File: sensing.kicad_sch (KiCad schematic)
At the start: 0 parts

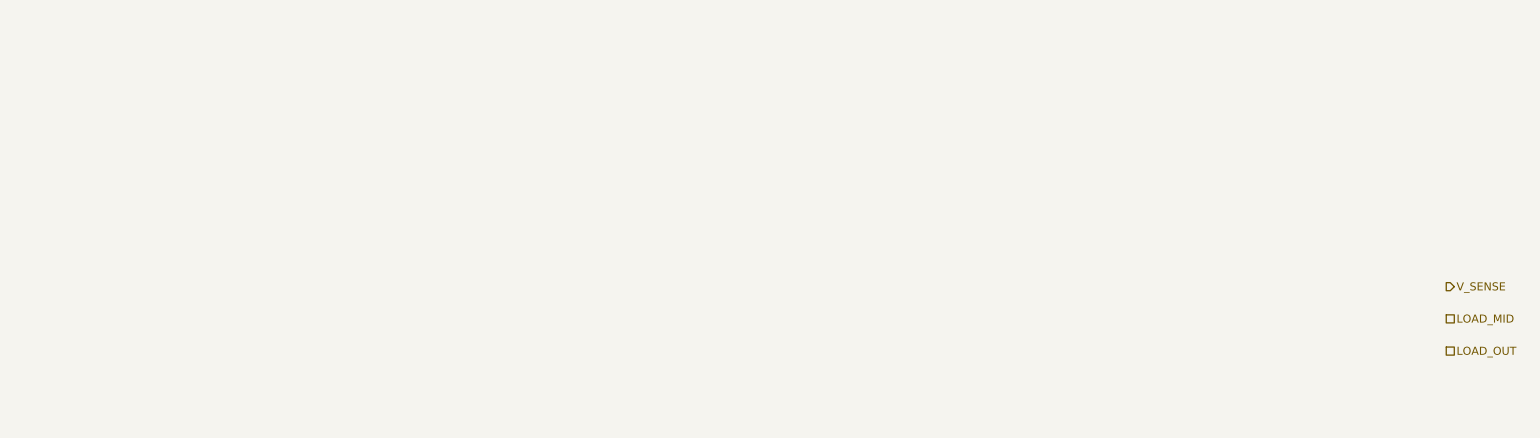
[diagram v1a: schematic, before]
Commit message: Add current sensing sheet
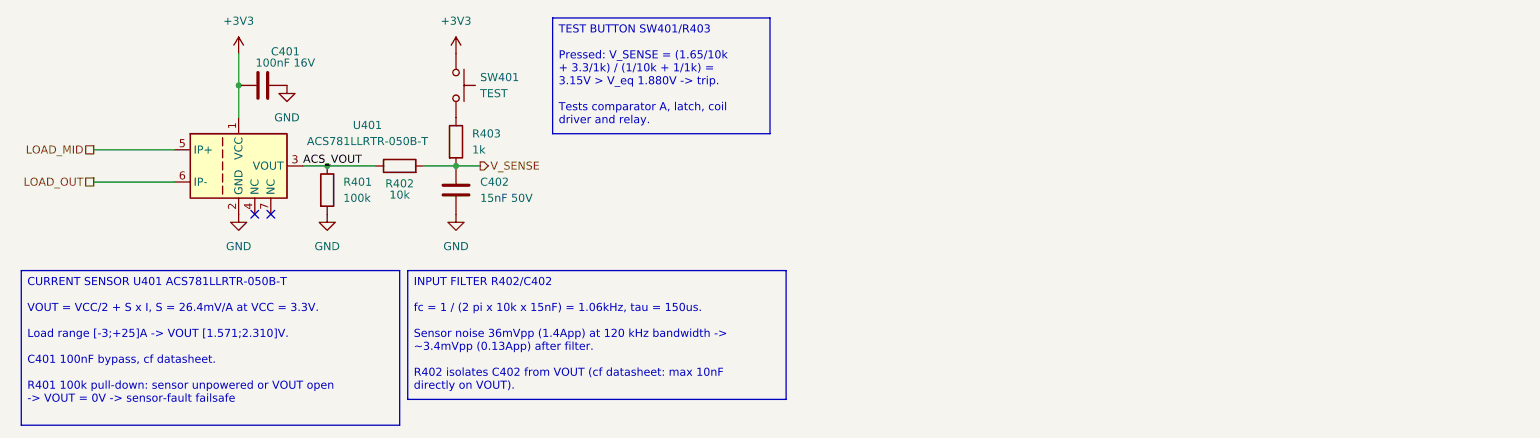
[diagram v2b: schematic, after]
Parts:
- added C401: 100nF 16V, Capacitor_SMD:C_0603_1608Metric, symbol Device:C
- added C402: 15nF 50V, Capacitor_SMD:C_0603_1608Metric, symbol Device:C
- added R401: 100k, Resistor_SMD:R_0603_1608Metric, symbol Device:R
- added R402: 10k, Resistor_SMD:R_0603_1608Metric, symbol Device:R
- added R403: 1k, Resistor_SMD:R_0603_1608Metric, symbol Device:R
- added SW401: TEST, Button_Switch_SMD:Nidec_Copal_CAS-120A, symbol Switch:SW_Push
- added U401: ACS781LLRTR-050B-T, Sensor_Current:Allegro_PSOF-7_4.8x6.4mm_P1.60mm, symbol monitor:ACS781LLRTR-050B-T
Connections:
- net LOAD_MID: now also U401.5 (IP+)
- net LOAD_OUT: now also U401.6 (IP-)
- net V_SENSE: now also C402.1, R402.2, R403.2
- new net: R403.1, SW401.2
- new net +3V3: C401.1, SW401.1, U401.1 (VCC)
- new net ACS_VOUT: R401.1, R402.1, U401.3 (VOUT)
- new net GND: C401.2, C402.2, R401.2, U401.2 (GND)
- no-connect marks 0 -> 2

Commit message: Add current sensing sheet
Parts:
- added TP401: V_SENSE, TestPoint:TestPoint_Pad_D1.5mm, symbol Connector:TestPoint
- C402: value 15nF 50V -> 15nF 50V C0G
- SW401: footprint Button_Switch_SMD:Nidec_Copal_CAS-120A -> Button_Switch_SMD:SW_SPST_PTS645Sx43SMTR92
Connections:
- net V_SENSE: now also TP401.1
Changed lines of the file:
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@@
+		(color 0 0 0 0)
+	)
+	(junction
+		(at 100.33 38.1)
+		(diameter 0)
 		(color 0 0 0 0)
 	)
@@
 	(wire
 		(pts
-			(xy 88.9 38.1) (xy 85.09 38.1)
+			(xy 100.33 38.1) (xy 85.09 38.1)
+		)
+		(stroke
+			(width 0)
+			(type default)
+		)
+	)
+	(wire
+		(pts
+			(xy 105.41 38.1) (xy 100.33 38.1)
 		)
 		(stroke
@@
 	(hierarchical_label "V_SENSE"
 		(shape output)
-		(at 88.9 38.1 0)
+		(at 105.41 38.1 0)
 		(effects
 			(font
@@
 			)
 		)
-		(property "Footprint" "Button_Switch_SMD:Nidec_Copal_CAS-120A"
+		(property "Footprint" "Button_Switch_SMD:SW_SPST_PTS645Sx43SMTR92"
 			(at 90.17 25.4 0)
 			(hide yes)
@@
 			)
 		)
-		(property "Value" "15nF 50V"
+		(property "Value" "15nF 50V C0G"
 			(at 88.9 43.1799 0)
 			(show_name no)
@@
 					(unit 1)
 				)
+			)
+		)
+	)
+	(symbol
+		(lib_id "Connector:TestPoint")
+		(at 100.33 38.1 180)
+		(unit 1)
+		(body_style 1)
+		(exclude_from_sim no)
+		(in_bom yes)
+		(on_board yes)
+		(in_pos_files yes)
+		(dnp no)
+		(fields_autoplaced yes)
+		(property "Reference" "TP401"
+			(at 102.87 40.1319 0)
+			(show_name no)
+			(do_not_autoplace no)
+			(effects
+				(font
+					(size 1.27 1.27)
+				)
+				(justify right)
+			)
+		)
+		(property "Value" "V_SENSE"
+			(at 102.87 42.6719 0)
+			(show_name no)
+			(do_not_autoplace no)
+			(effects
+				(font
+					(size 1.27 1.27)
+				)
+				(justify right)
+			)
+		)
+		(property "Footprint" "TestPoint:TestPoint_Pad_D1.5mm"
+			(at 95.25 38.1 0)
+			(hide yes)
+			(show_name no)
+			(do_not_autoplace no)
+			(effects
+				(font
+					(size 1.27 1.27)
+				)
+			)
+		)
+		(property "Datasheet" ""
+			(at 95.25 38.1 0)
+			(hide yes)
+			(show_name no)
+			(do_not_autoplace no)
+			(effects
+				(font
+					(size 1.27 1.27)
+				)
+			)
+		)
+		(property "Description" "test point"
+			(at 100.33 38.1 0)
+			(hide yes)
+			(show_name no)
+			(do_not_autoplace no)
+			(effects
+				(font
+					(size 1.27 1.27)
+				)
+			)
+		)
+		(pin "1"
+		)
+		(instances
+			(project "recruitment"
+				(path "/bdc7face-9f7c-4701-80bb-4cc144448db1/5e39fbe6-f2b2-47d6-b0cb-2f6fe7168007"
+					(reference "TP401")
+					(unit 1)
+				)
